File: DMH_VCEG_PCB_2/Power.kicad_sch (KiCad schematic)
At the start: 14 parts, among them J0 Conn_01x01, J100 IDC_02x05, J101 IDC_02x08

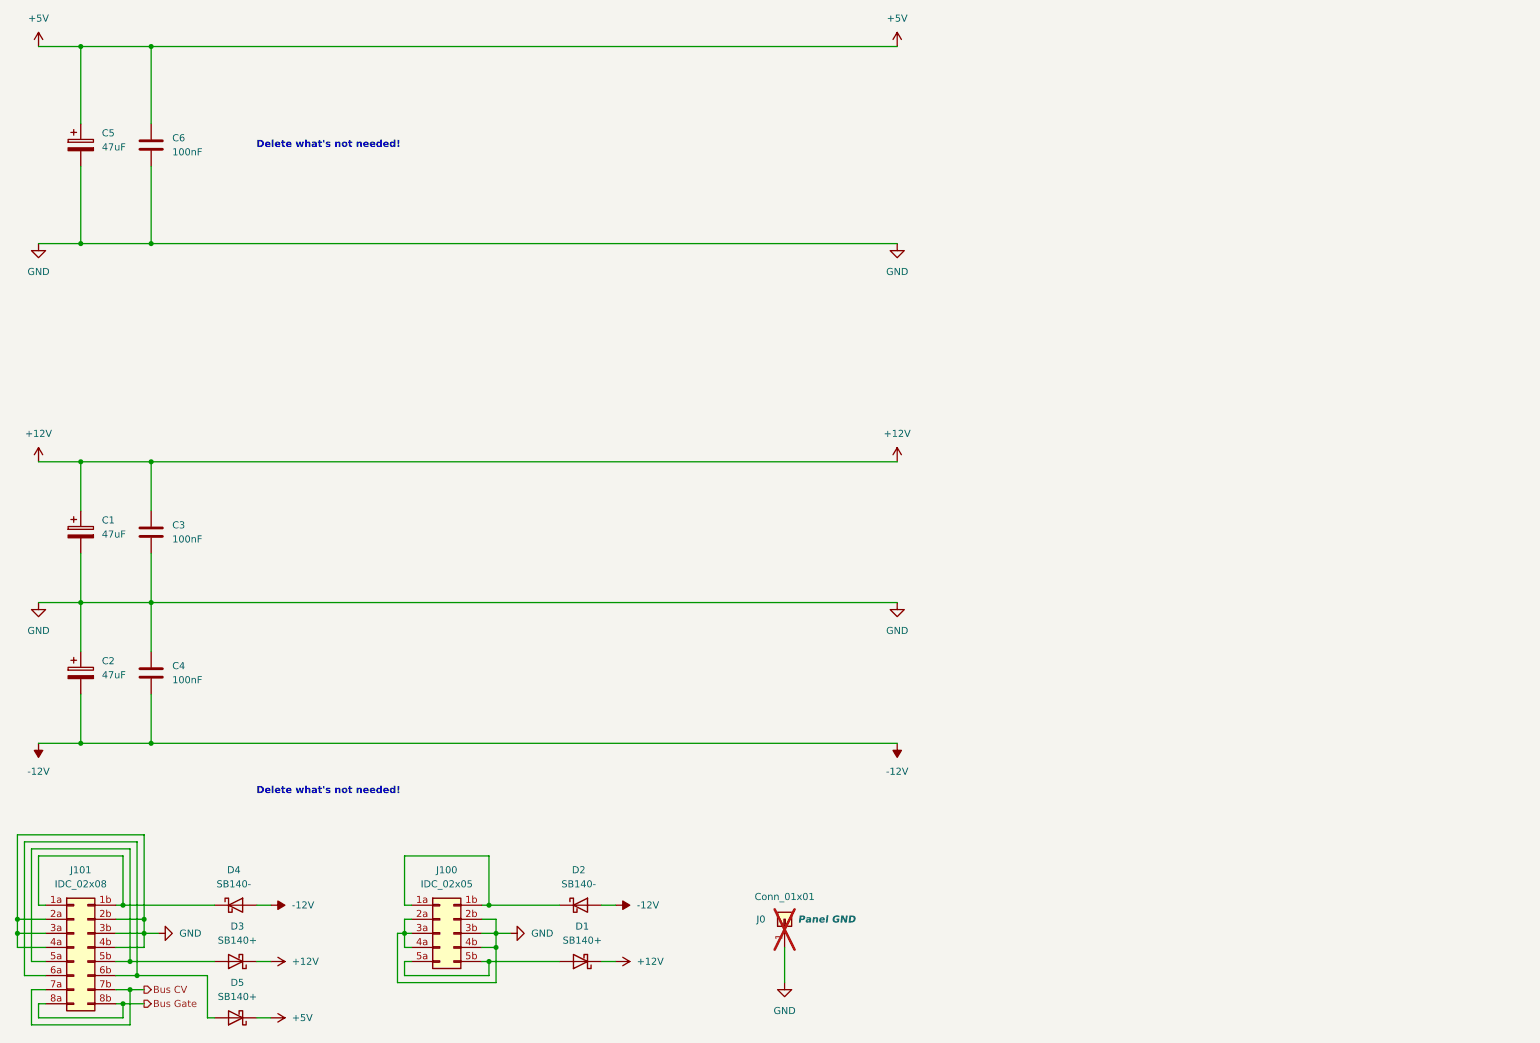
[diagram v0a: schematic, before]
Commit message: Copied PCB 1 as PCB 2
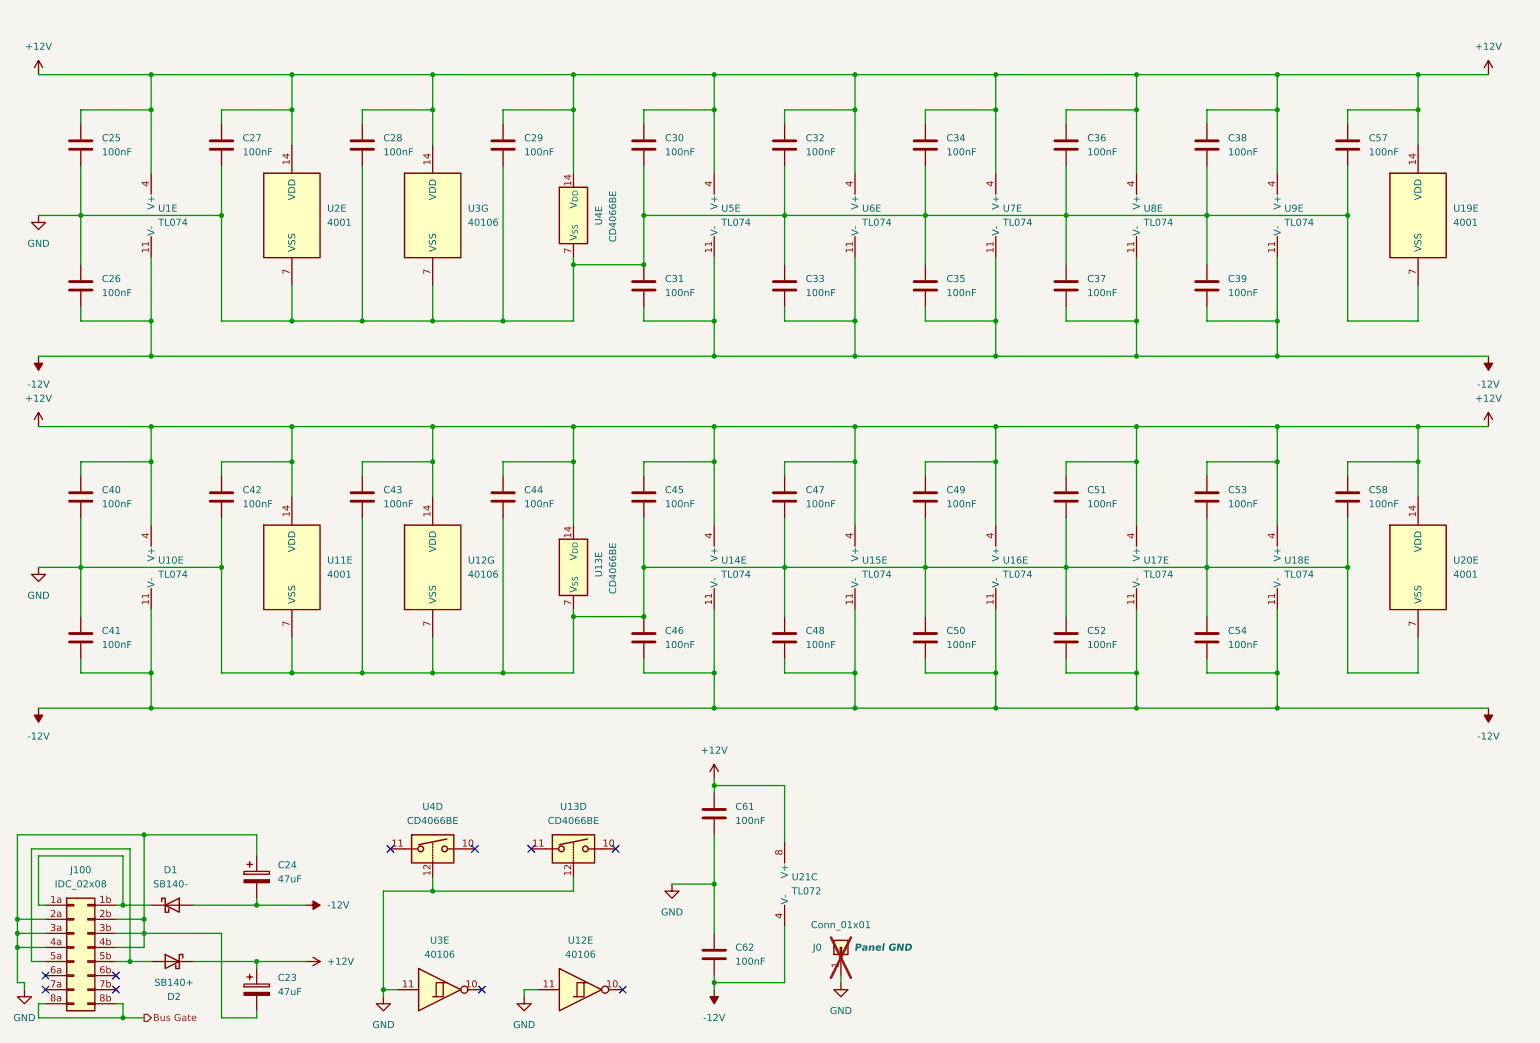
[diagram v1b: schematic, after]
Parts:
- removed C5: 47uF, Capacitor_THT:CP_Radial_D4.0mm_P1.50mm, symbol Device:C_Polarized
- removed C6: 100nF, Capacitor_THT:C_Disc_D4.3mm_W1.9mm_P5.00mm, symbol Device:C
- removed D1, D5: SB140+, Diode_THT:D_DO-41_SOD81_P10.16mm_Horizontal, symbol SynthStuff:Power_Bus_Schotty_+
- removed D2: SB140-, Diode_THT:D_DO-41_SOD81_P10.16mm_Horizontal, symbol SynthStuff:Power_Bus_Schotty_-
- removed J100: IDC_02x05, SynthStuff:IDC-Header_2x05_P2.54mm_Vertical_Eurorack, symbol SynthStuff:Eurorack_Power_Connector_10Pin
- added C27, C28, C29, C30, C31, C32, C33, C34, C35, C36, C37, C38, C39, C40, C41, C42, C43, C44, C45, C46, C47, C48, C49, C50, C51, C52, C53, C54, C57, C58, C61, C62: 100nF, Capacitor_THT:C_Disc_D4.3mm_W1.9mm_P5.00mm, symbol Device:C
- added U1, U10, U14, U15, U16, U17, U18, U5, U6, U7, U8, U9: TL074, Package_DIP:DIP-14_W7.62mm_Socket, symbol Amplifier_Operational:TL074
- added U11, U19, U2, U20: 4001, Package_DIP:DIP-14_W7.62mm_Socket, symbol 4xxx:4001
- added U12, U3: 40106, Package_DIP:DIP-14_W7.62mm_Socket, symbol 4xxx:40106
- added U13, U4: CD4066BE, Package_DIP:DIP-14_W7.62mm, symbol Analog_Switch:CD4066BE
- added U21: TL072, Package_DIP:DIP-8_W7.62mm, symbol Amplifier_Operational:TL072
- renumbered C1 to C23, C2 to C24, C3 to C25, C4 to C26, D4 to D1, D3 to D2, J101 to J100
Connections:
- net +12V: now also C27.1, C28.1, C29.1, C30.1, C32.1, C34.1, C36.1, C38.1, C40.1, C42.1, C43.1, C44.1, C45.1, C47.1, C49.1, C51.1, C53.1, C57.1, C58.1, C61.1, U1.4 (V+), U10.4 (V+), U11.14 (VDD), U12.14 (VDD), U13.14 (V_{DD}), U14.4 (V+), U15.4 (V+), U16.4 (V+), U17.4 (V+), U18.4 (V+), U19.14 (VDD), U2.14 (VDD), U20.14 (VDD), U21.8 (V+), U3.14 (VDD), U4.14 (V_{DD}), U5.4 (V+), U6.4 (V+), U7.4 (V+), U8.4 (V+), U9.4 (V+)
- net -12V: now also C31.2, C33.2, C35.2, C37.2, C39.2, C41.2, C46.2, C48.2, C50.2, C52.2, C54.2, C62.2, U1.11 (V-), U10.11 (V-), U14.11 (V-), U15.11 (V-), U16.11 (V-), U17.11 (V-), U18.11 (V-), U21.4 (V-), U5.11 (V-), U6.11 (V-), U7.11 (V-), U8.11 (V-), U9.11 (V-)
- net GND: now also C27.2, C28.2, C29.2, C30.2, C31.1, C32.2, C33.1, C34.2, C35.1, C36.2, C37.1, C38.2, C39.1, C40.2, C41.1, C42.2, C43.2, C44.2, C45.2, C46.1, C47.2, C48.1, C49.2, C50.1, C51.2, C52.1, C53.2, C54.1, C57.2, C58.2, C61.2, C62.1, U11.7 (VSS), U12.11, U12.7 (VSS), U13.12, U13.7 (V_{SS}), U19.7 (VSS), U2.7 (VSS), U20.7 (VSS), U3.11, U3.7 (VSS), U4.12, U4.7 (V_{SS})
- net at J100.6a (Pin_6a): no longer J100.6b (Pin_6b)
- net Bus CV: no longer names the net of J100.7a (Pin_7a)
- net Bus CV: no longer J100.7b (Pin_7b)
- no-connect marks 0 -> 10
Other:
- note removed: "Delete what's not needed!"
- moved on the sheet: C23, C24, C25, C26, D1, D2, J0

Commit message: Placed front panel components on PCB 2
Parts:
- J0: Function Panel GND -> GND
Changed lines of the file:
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@@
 		(exclude_from_sim no)
 		(in_bom yes)
-		(on_board no)
+		(on_board yes)
 		(dnp no)
 		(fields_autoplaced yes)
@@
 		(exclude_from_sim no)
 		(in_bom yes)
-		(on_board yes)
+		(on_board no)
 		(dnp no)
 		(fields_autoplaced yes)
@@
 		(exclude_from_sim no)
 		(in_bom yes)
-		(on_board yes)
+		(on_board no)
 		(dnp no)
 		(fields_autoplaced yes)
@@
 		(exclude_from_sim no)
 		(in_bom yes)
-		(on_board no)
+		(on_board yes)
 		(dnp no)
 		(fields_autoplaced yes)
@@
 		(exclude_from_sim no)
 		(in_bom yes)
-		(on_board yes)
+		(on_board no)
 		(dnp no)
 		(fields_autoplaced yes)
@@
 		(exclude_from_sim no)
 		(in_bom yes)
-		(on_board yes)
+		(on_board no)
 		(dnp no)
 		(fields_autoplaced yes)
@@
 		(exclude_from_sim no)
 		(in_bom yes)
-		(on_board yes)
+		(on_board no)
 		(dnp no)
 		(fields_autoplaced yes)
@@
 		(exclude_from_sim no)
 		(in_bom yes)
-		(on_board no)
+		(on_board yes)
 		(dnp no)
 		(fields_autoplaced yes)
@@
 		(exclude_from_sim no)
 		(in_bom yes)
-		(on_board yes)
+		(on_board no)
 		(dnp no)
 		(fields_autoplaced yes)
@@
 		(exclude_from_sim no)
 		(in_bom yes)
-		(on_board yes)
+		(on_board no)
 		(dnp no)
 		(fields_autoplaced yes)
@@
 		(exclude_from_sim no)
 		(in_bom yes)
-		(on_board no)
+		(on_board yes)
 		(dnp no)
 		(fields_autoplaced yes)
@@
 		(exclude_from_sim no)
 		(in_bom yes)
-		(on_board yes)
+		(on_board no)
 		(dnp no)
 		(fields_autoplaced yes)
@@
 		(exclude_from_sim no)
 		(in_bom yes)
-		(on_board yes)
+		(on_board no)
 		(dnp no)
 		(fields_autoplaced yes)
@@
 		(exclude_from_sim no)
 		(in_bom yes)
-		(on_board yes)
+		(on_board no)
 		(dnp no)
 		(fields_autoplaced yes)
@@
 		(exclude_from_sim no)
 		(in_bom yes)
-		(on_board no)
+		(on_board yes)
 		(dnp no)
 		(fields_autoplaced yes)
@@
 		(exclude_from_sim no)
 		(in_bom yes)
-		(on_board no)
+		(on_board yes)
 		(dnp no)
 		(fields_autoplaced yes)
@@
 		(exclude_from_sim no)
 		(in_bom yes)
-		(on_board yes)
+		(on_board no)
 		(dnp no)
 		(fields_autoplaced yes)
@@
 		(exclude_from_sim no)
 		(in_bom yes)
-		(on_board yes)
+		(on_board no)
 		(dnp no)
 		(fields_autoplaced yes)
@@
 		(exclude_from_sim no)
 		(in_bom yes)
-		(on_board no)
+		(on_board yes)
 		(dnp no)
 		(fields_autoplaced yes)
@@
 		(exclude_from_sim no)
 		(in_bom yes)
-		(on_board yes)
+		(on_board no)
 		(dnp no)
 		(fields_autoplaced yes)
@@
 		(exclude_from_sim no)
 		(in_bom yes)
-		(on_board yes)
+		(on_board no)
 		(dnp no)
 		(fields_autoplaced yes)
@@
 		(exclude_from_sim no)
 		(in_bom no)
-		(on_board no)
+		(on_board yes)
 		(dnp yes)
 		(property "Reference" "J0"
@@
 			)
 		)
-		(property "Function" "Panel GND"
-			(at 170.18 182.88 90)
+		(property "Function" "GND"
+			(at 167.132 182.88 90)
 			(effects
 				(font
@@
 		(exclude_from_sim no)
 		(in_bom yes)
-		(on_board yes)
+		(on_board no)
 		(dnp no)
 		(fields_autoplaced yes)
@@
 		(exclude_from_sim no)
 		(in_bom yes)
-		(on_board yes)
+		(on_board no)
 		(dnp no)
 		(fields_autoplaced yes)
@@
 		(exclude_from_sim no)
 		(in_bom yes)
-		(on_board yes)
+		(on_board no)
 		(dnp no)
 		(fields_autoplaced yes)
@@
 		(exclude_from_sim no)
 		(in_bom yes)
-		(on_board yes)
+		(on_board no)
 		(dnp no)
 		(fields_autoplaced yes)
@@
 		(exclude_from_sim no)
 		(in_bom yes)
-		(on_board yes)
+		(on_board no)
 		(dnp no)
 		(fields_autoplaced yes)
@@
 		(exclude_from_sim no)
 		(in_bom yes)
-		(on_board yes)
+		(on_board no)
 		(dnp no)
 		(fields_autoplaced yes)
@@
 		(exclude_from_sim no)
 		(in_bom yes)
-		(on_board no)
+		(on_board yes)
 		(dnp no)
 		(fields_autoplaced yes)
@@
 		(exclude_from_sim no)
 		(in_bom yes)
-		(on_board yes)
+		(on_board no)
 		(dnp no)
 		(fields_autoplaced yes)
@@
 		(exclude_from_sim no)
 		(in_bom yes)
-		(on_board yes)
+		(on_board no)
 		(dnp no)
 		(fields_autoplaced yes)
@@
 		(exclude_from_sim no)
 		(in_bom yes)
-		(on_board yes)
+		(on_board no)
 		(dnp no)
 		(fields_autoplaced yes)
@@
 		(exclude_from_sim no)
 		(in_bom yes)
-		(on_board yes)
+		(on_board no)
 		(dnp no)
 		(property "Reference" "U13"
@@
 		(exclude_from_sim no)
 		(in_bom yes)
-		(on_board no)
+		(on_board yes)
 		(dnp no)
 		(fields_autoplaced yes)
@@
 		(exclude_from_sim no)
 		(in_bom yes)
-		(on_board yes)
+		(on_board no)
 		(dnp no)
 		(fields_autoplaced yes)
@@
 		(exclude_from_sim no)
 		(in_bom yes)
-		(on_board no)
+		(on_board yes)
 		(dnp no)
 		(fields_autoplaced yes)
@@
 		(exclude_from_sim no)
 		(in_bom yes)
-		(on_board yes)
+		(on_board no)
 		(dnp no)
 		(fields_autoplaced yes)
@@
 		(exclude_from_sim no)
 		(in_bom yes)
-		(on_board no)
+		(on_board yes)
 		(dnp no)
 		(fields_autoplaced yes)
@@
 		(exclude_from_sim no)
 		(in_bom yes)
-		(on_board no)
+		(on_board yes)
 		(dnp no)
 		(fields_autoplaced yes)
@@
 		(exclude_from_sim no)
 		(in_bom yes)
-		(on_board yes)
+		(on_board no)
 		(dnp no)
 		(fields_autoplaced yes)
@@
 		(exclude_from_sim no)
 		(in_bom yes)
-		(on_board yes)
+		(on_board no)
 		(dnp no)
 		(fields_autoplaced yes)
@@
 		(exclude_from_sim no)
 		(in_bom yes)
-		(on_board no)
+		(on_board yes)
 		(dnp no)
 		(fields_autoplaced yes)
@@
 		(exclude_from_sim no)
 		(in_bom yes)
-		(on_board no)
+		(on_board yes)
 		(dnp no)
 		(fields_autoplaced yes)
@@
 		(exclude_from_sim no)
 		(in_bom yes)
-		(on_board yes)
+		(on_board no)
 		(dnp no)
 		(fields_autoplaced yes)
@@
 		(exclude_from_sim no)
 		(in_bom yes)
-		(on_board yes)
+		(on_board no)
 		(dnp no)
 		(fields_autoplaced yes)
@@
 		(exclude_from_sim no)
 		(in_bom yes)
-		(on_board yes)
+		(on_board no)
 		(dnp no)
 		(fields_autoplaced yes)
@@
 		(exclude_from_sim no)
 		(in_bom yes)
-		(on_board yes)
+		(on_board no)
 		(dnp no)
 		(fields_autoplaced yes)
@@
 		(exclude_from_sim no)
 		(in_bom yes)
-		(on_board yes)
+		(on_board no)
 		(dnp no)
 		(property "Reference" "D2"
@@
 		(exclude_from_sim no)
 		(in_bom yes)
-		(on_board yes)
+		(on_board no)
 		(dnp no)
 		(fields_autoplaced yes)
@@
 		(exclude_from_sim no)
 		(in_bom yes)
-		(on_board no)
+		(on_board yes)
 		(dnp no)
 		(fields_autoplaced yes)
@@
 		(exclude_from_sim no)
 		(in_bom yes)
-		(on_board yes)
+		(on_board no)
 		(dnp no)
 		(fields_autoplaced yes)
@@
 		(exclude_from_sim no)
 		(in_bom yes)
-		(on_board no)
+		(on_board yes)
 		(dnp no)
 		(fields_autoplaced yes)
@@
 		(exclude_from_sim no)
 		(in_bom yes)
-		(on_board yes)
+		(on_board no)
 		(dnp no)
 		(fields_autoplaced yes)
@@
 		(exclude_from_sim no)
 		(in_bom yes)
-		(on_board yes)
+		(on_board no)
 		(dnp no)
 		(property "Reference" "U4"
@@
 		(exclude_from_sim no)
 		(in_bom yes)
-		(on_board no)
+		(on_board yes)
 		(dnp no)
 		(fields_autoplaced yes)
@@
 		(exclude_from_sim no)
 		(in_bom yes)
-		(on_board no)
+		(on_board yes)
 		(dnp no)
 		(fields_autoplaced yes)
@@
 		(exclude_from_sim no)
 		(in_bom yes)
-		(on_board yes)
+		(on_board no)
 		(dnp no)
 		(fields_autoplaced yes)
@@
 		(exclude_from_sim no)
 		(in_bom yes)
-		(on_board yes)
+		(on_board no)
 		(dnp no)
 		(fields_autoplaced yes)
@@
 		(exclude_from_sim no)
 		(in_bom yes)
-		(on_board yes)
+		(on_board no)
 		(dnp no)
 		(fields_autoplaced yes)
@@
 		(exclude_from_sim no)
 		(in_bom yes)
-		(on_board no)
+		(on_board yes)
 		(dnp no)
 		(fields_autoplaced yes)
@@
 		(exclude_from_sim no)
 		(in_bom yes)
-		(on_board yes)
+		(on_board no)
 		(dnp no)
 		(fields_autoplaced yes)
@@
 		(exclude_from_sim no)
 		(in_bom yes)
-		(on_board no)
+		(on_board yes)
 		(dnp no)
 		(fields_autoplaced yes)
@@
 		(exclude_from_sim no)
 		(in_bom yes)
-		(on_board no)
+		(on_board yes)
 		(dnp no)
 		(fields_autoplaced yes)
@@
 		(exclude_from_sim no)
 		(in_bom yes)
-		(on_board yes)
+		(on_board no)
 		(dnp no)
 		(fields_autoplaced yes)
@@
 		(exclude_from_sim no)
 		(in_bom yes)
-		(on_board yes)
+		(on_board no)
 		(dnp no)
 		(fields_autoplaced yes)

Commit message: Placed ICs and pin headers on PCB 2
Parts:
- removed J0: Conn_01x01, Connector_PinHeader_2.54mm:PinHeader_1x01_P2.54mm_Vertical, symbol Connector_Generic:Conn_01x01
- U21: footprint Package_DIP:DIP-8_W7.62mm -> Package_DIP:DIP-8_W7.62mm_Socket
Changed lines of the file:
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@@
 	(wire
 		(pts
-			(xy 162.56 187.96) (xy 162.56 189.23)
-		)
-		(stroke
-			(width 0)
-			(type default)
-		)
-	)
-	(wire
-		(pts
 			(xy 241.3 58.42) (xy 241.3 69.85)
 		)
@@
 	)
 	(symbol
-		(lib_id "power:GND")
-		(at 162.56 189.23 0)
-		(unit 1)
-		(exclude_from_sim no)
-		(in_bom yes)
-		(on_board yes)
-		(dnp no)
-		(fields_autoplaced yes)
-		(property "Reference" "#PWR0118"
-			(at 162.56 195.58 0)
-			(effects
-				(font
-					(size 1.27 1.27)
-				)
-				(hide yes)
-			)
-		)
-		(property "Value" "GND"
-			(at 162.56 194.31 0)
-			(effects
-				(font
-					(size 1.27 1.27)
-				)
-			)
-		)
-		(property "Footprint" ""
-			(at 162.56 189.23 0)
-			(effects
-				(font
-					(size 1.27 1.27)
-				)
-				(hide yes)
-			)
-		)
-		(property "Datasheet" ""
-			(at 162.56 189.23 0)
-			(effects
-				(font
-					(size 1.27 1.27)
-				)
-				(hide yes)
-			)
-		)
-		(property "Description" "Power symbol creates a global label with name \"GND\" , ground"
-			(at 162.56 189.23 0)
-			(effects
-				(font
-					(size 1.27 1.27)
-				)
-				(hide yes)
-			)
-		)
-		(pin "1"
-		)
-		(instances
-			(project "DMH-Kosmo-10cm-PCB"
-				(path "/58f4306d-5387-4983-bb08-41a2313fd315/0cdf34b2-39cd-4d9e-981a-97cd34791509"
-					(reference "#PWR0118")
-					(unit 1)
-				)
-			)
-		)
-	)
-	(symbol
 		(lib_id "4xxx:4001")
 		(at 266.7 114.3 0)
@@
 	)
 	(symbol
-		(lib_id "Connector_Generic:Conn_01x01")
-		(at 162.56 182.88 90)
-		(unit 1)
-		(exclude_from_sim no)
-		(in_bom no)
-		(on_board yes)
-		(dnp yes)
-		(property "Reference" "J0"
-			(at 157.48 182.88 90)
-			(effects
-				(font
-					(size 1.27 1.27)
-				)
-				(justify right)
-			)
-		)
-		(property "Value" "Conn_01x01"
-			(at 162.56 178.816 90)
-			(effects
-				(font
-					(size 1.27 1.27)
-				)
-			)
-		)
-		(property "Footprint" "Connector_PinHeader_2.54mm:PinHeader_1x01_P2.54mm_Vertical"
-			(at 162.56 182.88 0)
-			(effects
-				(font
-					(size 1.27 1.27)
-				)
-				(hide yes)
-			)
-		)
-		(property "Datasheet" "~"
-			(at 162.56 182.88 0)
-			(effects
-				(font
-					(size 1.27 1.27)
-				)
-				(hide yes)
-			)
-		)
-		(property "Description" "Generic connector, single row, 01x01, script generated (kicad-library-utils/schlib/autogen/connector/)"
-			(at 162.56 182.88 0)
-			(effects
-				(font
-					(size 1.27 1.27)
-				)
-				(hide yes)
-			)
-		)
-		(property "Function" "GND"
-			(at 167.132 182.88 90)
-			(effects
-				(font
-					(size 1.27 1.27)
-					(thickness 0.254)
-					(bold yes)
-					(italic yes)
-				)
-			)
-		)
-		(pin "1"
-		)
-		(instances
-			(project "DMH-Kosmo-10cm-PCB"
-				(path "/58f4306d-5387-4983-bb08-41a2313fd315/0cdf34b2-39cd-4d9e-981a-97cd34791509"
-					(reference "J0")
-					(unit 1)
-				)
-			)
-		)
-	)
-	(symbol
 		(lib_id "Device:C")
 		(at 177.8 101.6 0)
@@
 		(exclude_from_sim no)
 		(in_bom yes)
-		(on_board yes)
+		(on_board no)
 		(dnp no)
 		(fields_autoplaced yes)
@@
 			)
 		)
-		(property "Footprint" "Package_DIP:DIP-8_W7.62mm"
+		(property "Footprint" "Package_DIP:DIP-8_W7.62mm_Socket"
 			(at 154.94 171.45 0)
 			(effects
@@
 		(exclude_from_sim no)
 		(in_bom yes)
-		(on_board yes)
+		(on_board no)
 		(dnp no)
 		(fields_autoplaced yes)

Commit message: Addition of manual gate ongoing
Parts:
- removed unit 5 of U12
- removed unit 5 of U3
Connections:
- no-connect marks 10 -> 8
